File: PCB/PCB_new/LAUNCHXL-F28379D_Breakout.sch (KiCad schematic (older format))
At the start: 21 parts, among them IC1 LM358N, J10 SERVO_CONN, J11 MC_CONN, Q1 220mA/50V/3.5Ω, Q2 100V/17A, Q3 100V/17A, Q4 100V/17A, Q5 100V/17A, Q6 100V/17A

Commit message: removed erroneous hidden traces
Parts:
- DCDC_CONN_12V: value 22-23-2021 -> DCDC_CONN
- FTDI: value CONN_06LONGPADS -> FTDI
- JETSON_CONN_PWR: value 22-23-2031 -> JETSON_CONN_PWR
- renumbered J10 to CONN
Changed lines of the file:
@@
 AR Path="/A664394C" Ref="FTDI"  Part="1"
 AR Path="/5DD5E236/A664394C" Ref="FTDI"  Part="1"
-AR Path="/5DF27AC1/A664394C" Ref="FTDI1"  Part="1"
-F 0 "FTDI1" H 1600 3920 70  0000 L BNN
-F 1 "CONN_06LONGPADS" H 1600 3110 70  0000 L BNN
+AR Path="/5DF27AC1/A664394C" Ref="CONN"  Part="1"
+F 0 "CONN" H 1400 3550 70  0000 L BNN
+F 1 "FTDI" H 1450 3350 70  0000 L BNN
 F 2 "Drivetrain_control:1X06_LONGPADS" H 1800 3500 50  0001 C CNN
 F 3 "" H 1800 3500 50  0001 C CNN
@@
 AR Path="/7CA1BA3F" Ref="JETSON_CONN_PWR"  Part="1"
 AR Path="/5DD5E236/7CA1BA3F" Ref="JETSON_CONN_PWR"  Part="1"
-AR Path="/5DF27AC1/7CA1BA3F" Ref="JETSON_CONN_PWR1"  Part="1"
-F 0 "JETSON_CONN_PWR1" H 9800 1400 51  0000 L BNN
-F 1 "22-23-2031" H 10470 1655 59  0001 L BNN
+AR Path="/5DF27AC1/7CA1BA3F" Ref="CONN"  Part="1"
+F 0 "CONN" H 10250 1450 51  0000 L BNN
+F 1 "JETSON_CONN_PWR" H 9600 1600 59  0000 L BNN
 F 2 "Drivetrain_control:22-23-2031" H 10500 1600 50  0001 C CNN
 F 3 "" H 10500 1600 50  0001 C CNN
@@
 check the package for this, needs to be SIL??\nSparkfun product specs
 $Comp
-L Connector:Conn_01x08_Male J10
+L Connector:Conn_01x08_Male CONN
 U 1 1 5DFE807D
 P 3200 1400
-F 0 "J10" H 3172 1282 50  0000 R CNN
+F 0 "CONN" H 3172 1282 50  0000 R CNN
 F 1 "SERVO_CONN" H 3172 1373 50  0000 R CNN
 F 2 "Drivetrain_control:5566-8" H 3200 1400 50  0001 C CNN
@@
 AR Path="/F0B3D357" Ref="DCDC_CONN_12V"  Part="1"
 AR Path="/5DD5E236/F0B3D357" Ref="DCDC_CONN_12V"  Part="1"
-AR Path="/5DF27AC1/F0B3D357" Ref="DCDC_CONN_12"  Part="1"
-F 0 "DCDC_CONN_12" H 6900 1450 51  0000 L BNN
-F 1 "22-23-2021" H 7570 1555 59  0001 L BNN
+AR Path="/5DF27AC1/F0B3D357" Ref="CONN"  Part="1"
+F 0 "CONN" H 7300 1400 51  0000 L BNN
+F 1 "DCDC_CONN" H 7000 1550 59  0000 L BNN
 F 2 "Drivetrain_control:22-23-2021" H 7600 1500 50  0001 C CNN
 F 3 "" H 7600 1500 50  0001 C CNN

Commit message: added ftdi 3d model and cleaned up .pretty folder
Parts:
- FTDI: footprint Drivetrain_control:1X06_LONGPADS -> Drivetrain_control:FTDI_CONN
- renumbered CONN to CONN2, J11 to CONN5
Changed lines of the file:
@@
 EESchema Schematic File Version 4
+LIBS:PCB_2020-cache
 EELAYER 30 0
 EELAYER END
@@
 $EndComp
 $Comp
-L Connector:Conn_01x06_Male FTDI
-U 1 1 A664394C
-P 1800 3500
-AR Path="/A664394C" Ref="FTDI"  Part="1"
-AR Path="/5DD5E236/A664394C" Ref="FTDI"  Part="1"
-AR Path="/5DF27AC1/A664394C" Ref="CONN"  Part="1"
-F 0 "CONN" H 1400 3550 70  0000 L BNN
-F 1 "FTDI" H 1450 3350 70  0000 L BNN
-F 2 "Drivetrain_control:1X06_LONGPADS" H 1800 3500 50  0001 C CNN
-F 3 "" H 1800 3500 50  0001 C CNN
-	1    1800 3500
-	1    0    0    -1
-$EndComp
-$Comp
 L power:+3V3 #+3V1
 U 1 1 612E3AAF
@@
 AR Path="/7CA1BA3F" Ref="JETSON_CONN_PWR"  Part="1"
 AR Path="/5DD5E236/7CA1BA3F" Ref="JETSON_CONN_PWR"  Part="1"
-AR Path="/5DF27AC1/7CA1BA3F" Ref="CONN"  Part="1"
-F 0 "CONN" H 10250 1450 51  0000 L BNN
+AR Path="/5DF27AC1/7CA1BA3F" Ref="CONN4"  Part="1"
+F 0 "CONN4" H 10250 1450 51  0000 L BNN
 F 1 "JETSON_CONN_PWR" H 9600 1600 59  0000 L BNN
 F 2 "Drivetrain_control:22-23-2031" H 10500 1600 50  0001 C CNN
@@
 Connector to Servo Motor
 $Comp
-L Connector:Conn_01x04_Male J11
+L Connector:Conn_01x04_Male CONN5
 U 1 1 5E01BD9E
 P 11150 4550
-F 0 "J11" H 11122 4432 50  0000 R CNN
+F 0 "CONN5" H 11122 4432 50  0000 R CNN
 F 1 "MC_CONN" H 11122 4523 50  0000 R CNN
 F 2 "Drivetrain_control:22-23-2041" H 11150 4550 50  0001 C CNN
@@
 check the package for this, needs to be SIL??\nSparkfun product specs
 $Comp
-L Connector:Conn_01x08_Male CONN
+L Connector:Conn_01x08_Male CONN2
 U 1 1 5DFE807D
 P 3200 1400
-F 0 "CONN" H 3172 1282 50  0000 R CNN
+F 0 "CONN2" H 3172 1282 50  0000 R CNN
 F 1 "SERVO_CONN" H 3172 1373 50  0000 R CNN
 F 2 "Drivetrain_control:5566-8" H 3200 1400 50  0001 C CNN
@@
 AR Path="/F0B3D357" Ref="DCDC_CONN_12V"  Part="1"
 AR Path="/5DD5E236/F0B3D357" Ref="DCDC_CONN_12V"  Part="1"
-AR Path="/5DF27AC1/F0B3D357" Ref="CONN"  Part="1"
-F 0 "CONN" H 7300 1400 51  0000 L BNN
+AR Path="/5DF27AC1/F0B3D357" Ref="CONN3"  Part="1"
+F 0 "CONN3" H 7300 1400 51  0000 L BNN
 F 1 "DCDC_CONN" H 7000 1550 59  0000 L BNN
 F 2 "Drivetrain_control:22-23-2021" H 7600 1500 50  0001 C CNN
@@
 	-1   0    0    1
 $EndComp
+$Comp
+L Connector:Conn_01x06_Male FTDI
+U 1 1 A664394C
+P 1800 3500
+AR Path="/A664394C" Ref="FTDI"  Part="1"
+AR Path="/5DD5E236/A664394C" Ref="FTDI"  Part="1"
+AR Path="/5DF27AC1/A664394C" Ref="CONN1"  Part="1"
+F 0 "CONN1" H 1400 3550 70  0000 L BNN
+F 1 "FTDI" H 1450 3350 70  0000 L BNN
+F 2 "Drivetrain_control:FTDI_CONN" H 1800 3500 50  0001 C CNN
+F 3 "" H 1800 3500 50  0001 C CNN
+	1    1800 3500
+	1    0    0    -1
+$EndComp
 $EndSCHEMATC

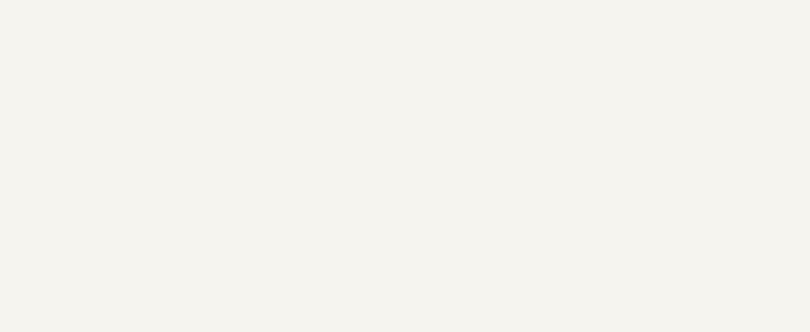
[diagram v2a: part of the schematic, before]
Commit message: created Brake_MC_Conn Footprint/model
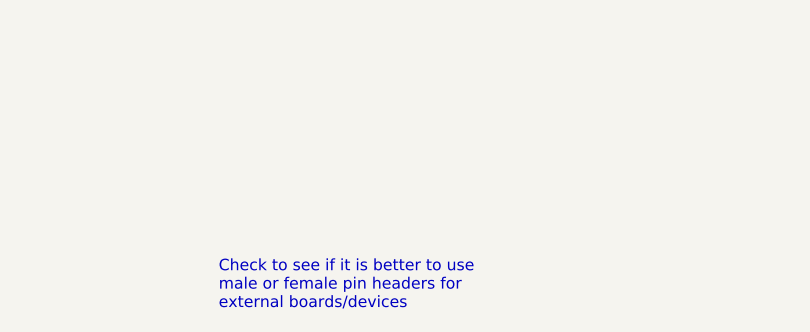
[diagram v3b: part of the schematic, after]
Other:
- note added: "Check to see if it is better to use\nmale or female pin headers for \nexternal boards/devices"
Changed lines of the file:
@@
 	1    0    0    -1
 $EndComp
+Text Notes 2250 7450 0    50   ~ 0
+Check to see if it is better to use\nmale or female pin headers for \nexternal boards/devices
 $EndSCHEMATC

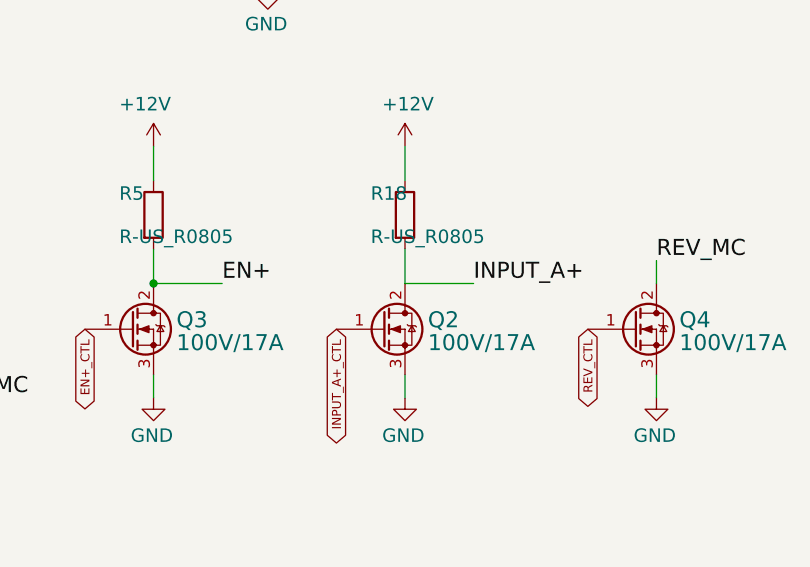
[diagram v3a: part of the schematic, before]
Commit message: updated footprints to kicad std lib and removed associated custom footprints
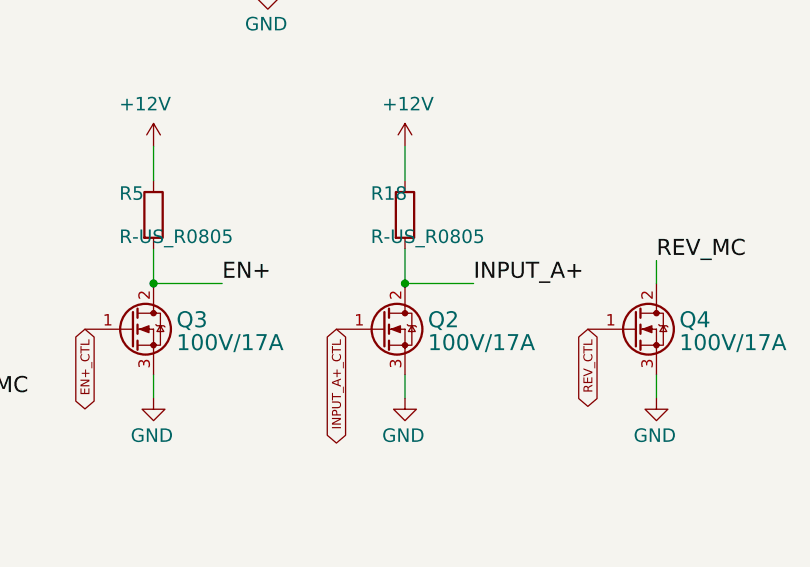
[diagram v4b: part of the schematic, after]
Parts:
- CONN2: footprint Drivetrain_control:5566-8 -> Connector_Molex:Molex_Mini-Fit_Jr_5566-08A2_2x04_P4.20mm_Vertical
- CONN5: footprint Drivetrain_control:22-23-2041 -> Connector_Molex:Molex_KK-254_AE-6410-04A_1x04_P2.54mm_Vertical
- DCDC_CONN_12V: footprint Drivetrain_control:22-23-2021 -> Connector_Molex:Molex_KK-254_AE-6410-02A_1x02_P2.54mm_Vertical
- IC1: footprint Drivetrain_control:DIL08 -> Package_DIP:DIP-8_W7.62mm_Socket
- JETSON_CONN_PWR: footprint Drivetrain_control:22-23-2031 -> Connector_Molex:Molex_KK-254_AE-6410-03A_1x03_P2.54mm_Vertical
- Q1: footprint Drivetrain_control:SOT23-3 -> Package_TO_SOT_SMD:SOT-23
- Q2, Q3, Q4, Q5, Q6: footprint Drivetrain_control:TO220V -> Package_TO_SOT_THT:TO-220-3_Vertical
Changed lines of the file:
@@
 F 0 "IC1" H 4700 3725 59  0001 L BNN
 F 1 "LM358N" H 4700 3400 59  0001 L BNN
-F 2 "Drivetrain_control:DIL08" H 4600 3600 50  0001 C CNN
+F 2 "Package_DIP:DIP-8_W7.62mm_Socket" H 4600 3600 50  0001 C CNN
 F 3 "" H 4600 3600 50  0001 C CNN
 	1    4600 3600
@@
 $EndComp
 $Comp
-L Device:Q_NMOS_GDS Q2
-U 1 1 BFFF77DC
-P 7700 3200
-AR Path="/BFFF77DC" Ref="Q2"  Part="1"
-AR Path="/5DD5E236/BFFF77DC" Ref="Q2"  Part="1"
-AR Path="/5DF27AC1/BFFF77DC" Ref="Q2"  Part="1"
-F 0 "Q2" H 7900 3200 70  0000 L BNN
-F 1 "100V/17A" H 7900 3100 70  0000 L BNN
-F 2 "Drivetrain_control:TO220V" H 7700 3200 50  0001 C CNN
-F 3 "" H 7700 3200 50  0001 C CNN
-	1    7700 3200
-	1    0    0    -1
-$EndComp
-$Comp
 L Device:R R18
 U 1 1 1A44BE4A
@@
 F 0 "CONN4" H 10250 1450 51  0000 L BNN
 F 1 "JETSON_CONN_PWR" H 9600 1600 59  0000 L BNN
-F 2 "Drivetrain_control:22-23-2031" H 10500 1600 50  0001 C CNN
+F 2 "Connector_Molex:Molex_KK-254_AE-6410-03A_1x03_P2.54mm_Vertical" H 10500 1600 50  0001 C CNN
 F 3 "" H 10500 1600 50  0001 C CNN
 	1    10500 1600
@@
 F 0 "Q3" H 6800 3200 70  0000 L BNN
 F 1 "100V/17A" H 6800 3100 70  0000 L BNN
-F 2 "Drivetrain_control:TO220V" H 6600 3200 50  0001 C CNN
-F 3 "" H 6600 3200 50  0001 C CNN
+F 2 "Package_TO_SOT_THT:TO-220-3_Vertical" H 6600 3200 50  0001 C CNN
+F 3 "https://www.infineon.com/dgdl/irl530npbf.pdf?fileId=5546d462533600a40153565fad5c2560" H 6600 3200 50  0001 C CNN
 	1    6600 3200
 	1    0    0    -1
 $EndComp
 Connection ~ 6700 3000
-$Comp
-L Device:Q_NMOS_GDS Q?
-U 1 1 5DF74B23
-P 8800 3200
-AR Path="/5DF74B23" Ref="Q?"  Part="1"
-AR Path="/5DD5E236/5DF74B23" Ref="Q?"  Part="1"
-AR Path="/5DF27AC1/5DF74B23" Ref="Q4"  Part="1"
-F 0 "Q4" H 9000 3200 70  0000 L BNN
-F 1 "100V/17A" H 9000 3100 70  0000 L BNN
-F 2 "Drivetrain_control:TO220V" H 8800 3200 50  0001 C CNN
-F 3 "" H 8800 3200 50  0001 C CNN
-	1    8800 3200
-	1    0    0    -1
-$EndComp
-$Comp
-L Device:Q_NMOS_GDS Q?
-U 1 1 5DF76A67
-P 9900 3200
-AR Path="/5DF76A67" Ref="Q?"  Part="1"
-AR Path="/5DD5E236/5DF76A67" Ref="Q?"  Part="1"
-AR Path="/5DF27AC1/5DF76A67" Ref="Q5"  Part="1"
-F 0 "Q5" H 10100 3200 70  0000 L BNN
-F 1 "100V/17A" H 10100 3100 70  0000 L BNN
-F 2 "Drivetrain_control:TO220V" H 9900 3200 50  0001 C CNN
-F 3 "" H 9900 3200 50  0001 C CNN
-	1    9900 3200
-	1    0    0    -1
-$EndComp
-$Comp
-L Device:Q_NMOS_GDS Q?
-U 1 1 5DF770F2
-P 11000 3200
-AR Path="/5DF770F2" Ref="Q?"  Part="1"
-AR Path="/5DD5E236/5DF770F2" Ref="Q?"  Part="1"
-AR Path="/5DF27AC1/5DF770F2" Ref="Q6"  Part="1"
-F 0 "Q6" H 11200 3200 70  0000 L BNN
-F 1 "100V/17A" H 11200 3100 70  0000 L BNN
-F 2 "Drivetrain_control:TO220V" H 11000 3200 50  0001 C CNN
-F 3 "" H 11000 3200 50  0001 C CNN
-	1    11000 3200
-	1    0    0    -1
-$EndComp
 Wire Wire Line
 	4300 4100 4550 4100
@@
 F 0 "CONN5" H 11122 4432 50  0000 R CNN
 F 1 "MC_CONN" H 11122 4523 50  0000 R CNN
-F 2 "Drivetrain_control:22-23-2041" H 11150 4550 50  0001 C CNN
+F 2 "Connector_Molex:Molex_KK-254_AE-6410-04A_1x04_P2.54mm_Vertical" H 11150 4550 50  0001 C CNN
 F 3 "~" H 11150 4550 50  0001 C CNN
 	1    11150 4550
@@
 F 0 "CONN2" H 3172 1282 50  0000 R CNN
 F 1 "SERVO_CONN" H 3172 1373 50  0000 R CNN
-F 2 "Drivetrain_control:5566-8" H 3200 1400 50  0001 C CNN
+F 2 "Connector_Molex:Molex_Mini-Fit_Jr_5566-08A2_2x04_P4.20mm_Vertical" H 3200 1400 50  0001 C CNN
 F 3 "~" H 3200 1400 50  0001 C CNN
 	1    3200 1400
@@
 F 0 "Q1" V 5600 1550 70  0000 L BNN
 F 1 "220mA/50V/3.5Ω" V 5700 1350 70  0000 L BNN
-F 2 "Drivetrain_control:SOT23-3" H 5300 1600 50  0001 C CNN
-F 3 "" H 5300 1600 50  0001 C CNN
+F 2 "Package_TO_SOT_SMD:SOT-23" H 5300 1600 50  0001 C CNN
+F 3 "https://www.onsemi.com/pub/Collateral/BSS138_F085-D.PDF" H 5300 1600 50  0001 C CNN
 	1    5300 1600
 	0    1    1    0
@@
 F 0 "CONN3" H 7300 1400 51  0000 L BNN
 F 1 "DCDC_CONN" H 7000 1550 59  0000 L BNN
-F 2 "Drivetrain_control:22-23-2021" H 7600 1500 50  0001 C CNN
+F 2 "Connector_Molex:Molex_KK-254_AE-6410-02A_1x02_P2.54mm_Vertical" H 7600 1500 50  0001 C CNN
 F 3 "" H 7600 1500 50  0001 C CNN
 	1    7600 1500
@@
 Text Notes 2250 7450 0    50   ~ 0
 Check to see if it is better to use\nmale or female pin headers for \nexternal boards/devices
+$Comp
+L Device:Q_NMOS_GDS Q?
+U 1 1 5E16D782
+P 7700 3200
+AR Path="/5E16D782" Ref="Q?"  Part="1"
+AR Path="/5DD5E236/5E16D782" Ref="Q?"  Part="1"
+AR Path="/5DF27AC1/5E16D782" Ref="Q2"  Part="1"
+F 0 "Q2" H 7900 3200 70  0000 L BNN
+F 1 "100V/17A" H 7900 3100 70  0000 L BNN
+F 2 "Package_TO_SOT_THT:TO-220-3_Vertical" H 7700 3200 50  0001 C CNN
+F 3 "https://www.infineon.com/dgdl/irl530npbf.pdf?fileId=5546d462533600a40153565fad5c2560" H 7700 3200 50  0001 C CNN
+	1    7700 3200
+	1    0    0    -1
+$EndComp
+Connection ~ 7800 3000
+$Comp
+L Device:Q_NMOS_GDS Q?
+U 1 1 5E16E676
+P 8800 3200
+AR Path="/5E16E676" Ref="Q?"  Part="1"
+AR Path="/5DD5E236/5E16E676" Ref="Q?"  Part="1"
+AR Path="/5DF27AC1/5E16E676" Ref="Q4"  Part="1"
+F 0 "Q4" H 9000 3200 70  0000 L BNN
+F 1 "100V/17A" H 9000 3100 70  0000 L BNN
+F 2 "Package_TO_SOT_THT:TO-220-3_Vertical" H 8800 3200 50  0001 C CNN
+F 3 "https://www.infineon.com/dgdl/irl530npbf.pdf?fileId=5546d462533600a40153565fad5c2560" H 8800 3200 50  0001 C CNN
+	1    8800 3200
+	1    0    0    -1
+$EndComp
+$Comp
+L Device:Q_NMOS_GDS Q?
+U 1 1 5E16EE89
+P 9900 3200
+AR Path="/5E16EE89" Ref="Q?"  Part="1"
+AR Path="/5DD5E236/5E16EE89" Ref="Q?"  Part="1"
+AR Path="/5DF27AC1/5E16EE89" Ref="Q5"  Part="1"
+F 0 "Q5" H 10100 3200 70  0000 L BNN
+F 1 "100V/17A" H 10100 3100 70  0000 L BNN
+F 2 "Package_TO_SOT_THT:TO-220-3_Vertical" H 9900 3200 50  0001 C CNN
+F 3 "https://www.infineon.com/dgdl/irl530npbf.pdf?fileId=5546d462533600a40153565fad5c2560" H 9900 3200 50  0001 C CNN
+	1    9900 3200
+	1    0    0    -1
+$EndComp
+$Comp
+L Device:Q_NMOS_GDS Q?
+U 1 1 5E16FA4A
+P 11000 3200
+AR Path="/5E16FA4A" Ref="Q?"  Part="1"
+AR Path="/5DD5E236/5E16FA4A" Ref="Q?"  Part="1"
+AR Path="/5DF27AC1/5E16FA4A" Ref="Q6"  Part="1"
+F 0 "Q6" H 11200 3200 70  0000 L BNN
+F 1 "100V/17A" H 11200 3100 70  0000 L BNN
+F 2 "Package_TO_SOT_THT:TO-220-3_Vertical" H 11000 3200 50  0001 C CNN
+F 3 "https://www.infineon.com/dgdl/irl530npbf.pdf?fileId=5546d462533600a40153565fad5c2560" H 11000 3200 50  0001 C CNN
+	1    11000 3200
+	1    0    0    -1
+$EndComp
 $EndSCHEMATC

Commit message: added ti 3d model to footprint
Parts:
- DCDC_CONN_12V: footprint Connector_Molex:Molex_KK-254_AE-6410-02A_1x02_P2.54mm_Vertical -> Connector_Molex:Molex_Mini-Fit_Jr_5566-02A_2x01_P4.20mm_Vertical
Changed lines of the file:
@@
 F 0 "CONN3" H 7300 1400 51  0000 L BNN
 F 1 "DCDC_CONN" H 7000 1550 59  0000 L BNN
-F 2 "Connector_Molex:Molex_KK-254_AE-6410-02A_1x02_P2.54mm_Vertical" H 7600 1500 50  0001 C CNN
+F 2 "Connector_Molex:Molex_Mini-Fit_Jr_5566-02A_2x01_P4.20mm_Vertical" H 7600 1500 50  0001 C CNN
 F 3 "" H 7600 1500 50  0001 C CNN
 	1    7600 1500

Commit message: added braking signals
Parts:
- added CONN6: Brake_CONN, Drivetrain_control:Brake_MC_Conn, symbol Connector:Conn_01x06_Male
- added CONN7: MC_CONN, Connector_Molex:Molex_KK-254_AE-6410-02A_1x02_P2.54mm_Vertical, symbol Connector:Conn_01x02_Male
- R18, R5: value R-US_R0805 -> 560
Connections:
- net labels added: Brake_Out_1, Brake_Out_2, Brake_PWM_1, Brake_PWM_2
- wire segments 73 -> 77
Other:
- note added: "resistor code is either 195 - 1.9M ohms\nor 561 - 560 ohms"
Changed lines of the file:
@@
 AR Path="/5DF27AC1/325BC02B" Ref="R5"  Part="1"
 F 0 "R5" H 6550 2759 59  0000 L BNN
-F 1 "R-US_R0805" H 6550 2570 59  0000 L BNN
+F 1 "560" H 6550 2570 59  0000 L BNN
 F 2 "Resistor_SMD:R_0805_2012Metric_Pad1.15x1.40mm_HandSolder" H 6700 2700 50  0001 C CNN
 F 3 "" H 6700 2700 50  0001 C CNN
@@
 AR Path="/5DF27AC1/1A44BE4A" Ref="R18"  Part="1"
 F 0 "R18" H 7650 2759 59  0000 L BNN
-F 1 "R-US_R0805" H 7650 2570 59  0000 L BNN
+F 1 "560" H 7650 2570 59  0000 L BNN
 F 2 "Resistor_SMD:R_0805_2012Metric_Pad1.15x1.40mm_HandSolder" H 7800 2700 50  0001 C CNN
 F 3 "" H 7800 2700 50  0001 C CNN
@@
 	1    0    0    -1
 $EndComp
+$Comp
+L Connector:Conn_01x06_Male CONN6
+U 1 1 5E187579
+P 5250 6100
+F 0 "CONN6" H 5358 6481 50  0000 C CNN
+F 1 "Brake_CONN" H 5358 6390 50  0000 C CNN
+F 2 "Drivetrain_control:Brake_MC_Conn" H 5250 6100 50  0001 C CNN
+F 3 "https://cdn-shop.adafruit.com/product-files/3190/drv8871.pdf" H 5250 6100 50  0001 C CNN
+F 4 "https://learn.adafruit.com/adafruit-drv8871-brushed-dc-motor-driver-breakout/" H 5250 6100 50  0001 C CNN "Website"
+	1    5250 6100
+	1    0    0    -1
+$EndComp
+Text GLabel 5450 5900 2    39   Input ~ 0
+Brake_PWM_2
+Text GLabel 5450 6000 2    39   Input ~ 0
+Brake_PWM_1
+$Comp
+L power:GND #GND?
+U 1 1 5E188E1D
+P 6100 6250
+AR Path="/5E188E1D" Ref="#GND?"  Part="1"
+AR Path="/5DD5E236/5E188E1D" Ref="#GND?"  Part="1"
+AR Path="/5DF27AC1/5E188E1D" Ref="#GND0101"  Part="1"
+F 0 "#GND0101" H 6100 6250 50  0001 C CNN
+F 1 "GND" H 6000 6050 59  0000 L BNN
+F 2 "" H 6100 6250 50  0001 C CNN
+F 3 "" H 6100 6250 50  0001 C CNN
+	1    6100 6250
+	1    0    0    -1
+$EndComp
+$Comp
+L power:+12V #P+?
+U 1 1 5E189D98
+P 6100 6050
+AR Path="/5E189D98" Ref="#P+?"  Part="1"
+AR Path="/5DD5E236/5E189D98" Ref="#P+?"  Part="1"
+AR Path="/5DF27AC1/5E189D98" Ref="#P+0101"  Part="1"
+F 0 "#P+0101" H 6100 6050 50  0001 C CNN
+F 1 "+12V" H 6000 6200 59  0000 L BNN
+F 2 "" H 6100 6050 50  0001 C CNN
+F 3 "" H 6100 6050 50  0001 C CNN
+	1    6100 6050
+	1    0    0    -1
+$EndComp
+Wire Wire Line
+	5450 6100 6100 6100
+Wire Wire Line
+	6100 6100 6100 6050
+Wire Wire Line
+	5450 6200 6100 6200
+Wire Wire Line
+	6100 6200 6100 6250
+Text Label 5450 6300 0    39   ~ 0
+Brake_Out_1
+Text Label 5450 6400 0    39   ~ 0
+Brake_Out_2
+Text Label 7100 6150 2    39   ~ 0
+Brake_Out_1
+Text Label 7100 6250 2    39   ~ 0
+Brake_Out_2
+$Comp
+L Connector:Conn_01x02_Male CONN7
+U 1 1 5E1945B9
+P 7300 6250
+F 0 "CONN7" H 7272 6132 50  0000 R CNN
+F 1 "MC_CONN" H 7272 6223 50  0000 R CNN
+F 2 "Connector_Molex:Molex_KK-254_AE-6410-02A_1x02_P2.54mm_Vertical" H 7300 6250 50  0001 C CNN
+F 3 "~" H 7300 6250 50  0001 C CNN
+	1    7300 6250
+	-1   0    0    1
+$EndComp
+Text Notes 7700 4150 2    39   ~ 0
+resistor code is either 195 - 1.9M ohms\nor 561 - 560 ohms
 $EndSCHEMATC

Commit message: updated component values
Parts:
- R3: value R-US_R0805 -> 3k
- R4: value R-US_R0805 -> 6.8k
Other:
- note added: "These resistors are chosen to get 10/3 gain"
- note removed: "Check to make sure that the mollex connection is correct for these!!"
- note removed: "Check to see if it is better to use\nmale or female pin headers for \nexternal boards/devices"
- note removed: "check this mollex connector too!!"
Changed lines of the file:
@@
 Wire Wire Line
 	10300 1700 10200 1700
-Text Label 5450 3500 0    70   ~ 0
+Text Label 5600 3500 0    70   ~ 0
 THROTTLE_MC
 Text Label 10950 4650 2    39   ~ 0
@@
 AR Path="/5DD5E236/D7A12E91" Ref="R4"  Part="1"
 AR Path="/5DF27AC1/D7A12E91" Ref="R4"  Part="1"
-F 0 "R4" V 4600 4200 59  0000 L BNN
-F 1 "R-US_R0805" V 4600 3550 59  0000 L BNN
+F 0 "R4" V 4800 4050 59  0000 L BNN
+F 1 "6.8k" V 4600 4000 59  0000 L BNN
 F 2 "Resistor_SMD:R_0805_2012Metric_Pad1.15x1.40mm_HandSolder" H 4700 4100 50  0001 C CNN
 F 3 "" H 4700 4100 50  0001 C CNN
@@
 AR Path="/5DD5E236/7A1EFB6B" Ref="R16"  Part="1"
 AR Path="/5DF27AC1/7A1EFB6B" Ref="R16"  Part="1"
-F 0 "R16" V 1750 1609 59  0000 L BNN
+F 0 "R16" H 1650 1600 59  0000 L BNN
 F 1 "R-US_R0805" V 2050 1400 59  0000 L BNN
 F 2 "Resistor_SMD:R_0805_2012Metric_Pad1.15x1.40mm_HandSolder" H 1900 1550 50  0001 C CNN
@@
 AR Path="/5DF27AC1/D43D5682" Ref="R3"  Part="1"
 F 0 "R3" H 4150 4459 59  0000 L BNN
-F 1 "R-US_R0805" H 4150 4270 59  0000 L BNN
+F 1 "3k" H 4150 4270 59  0000 L BNN
 F 2 "Resistor_SMD:R_0805_2012Metric_Pad1.15x1.40mm_HandSolder" H 4300 4400 50  0001 C CNN
 F 3 "" H 4300 4400 50  0001 C CNN
@@
 Wire Wire Line
 	10200 1700 10200 1900
-Text Notes 10150 900  0    50   ~ 10
-Check to make sure that the mollex connection is correct for these!!
-Text Notes 7700 1150 0    50   ~ 10
-check this mollex connector too!!
 Text Notes 2250 750  0    50   ~ 10
 check size of molex connector
@@
 	1    0    0    -1
 $EndComp
-Text Notes 2250 7450 0    50   ~ 0
-Check to see if it is better to use\nmale or female pin headers for \nexternal boards/devices
 $Comp
 L Device:Q_NMOS_GDS Q?
@@
 Text Notes 7700 4150 2    39   ~ 0
 resistor code is either 195 - 1.9M ohms\nor 561 - 560 ohms
+Text Notes 4950 5100 2    39   ~ 0
+These resistors are chosen to get 10/3 gain
 $EndSCHEMATC
